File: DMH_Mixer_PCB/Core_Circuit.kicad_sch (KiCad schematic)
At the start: 31 parts, among them SW1 SW_SPDT_321, SW2 SW_SPDT_321, SW3 SW_SPDT_321, SW4 SW_SPDT_321, SW5 SW_DPDT, U1 TL072

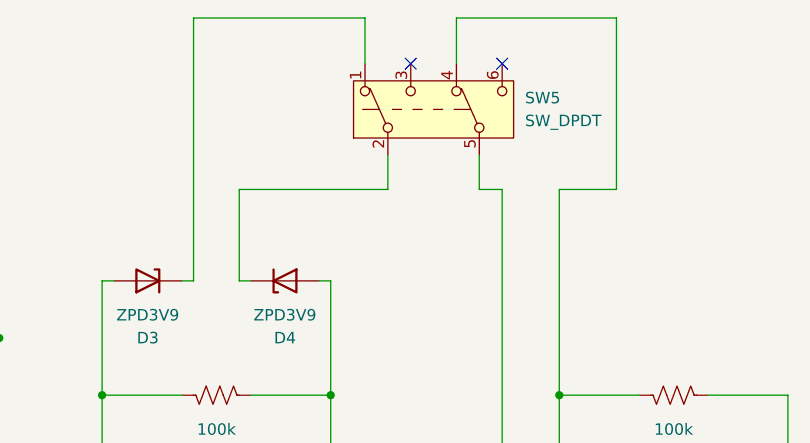
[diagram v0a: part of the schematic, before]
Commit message: PCB Component placement ready
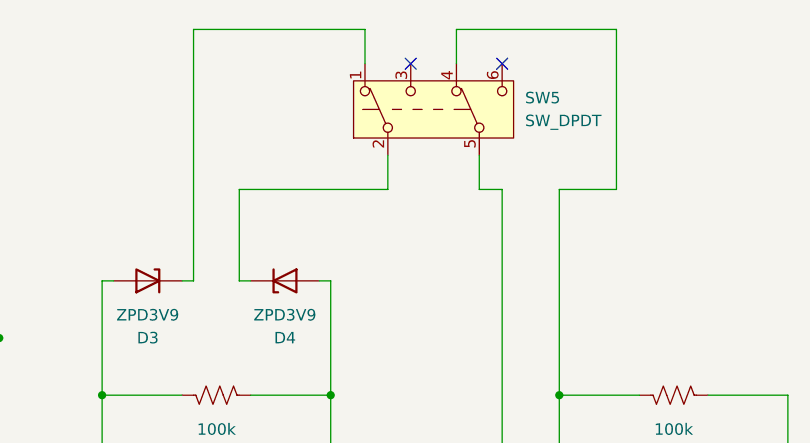
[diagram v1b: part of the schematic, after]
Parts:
- SW5: footprint SynthStuff:PinHeader_2x03_P2.54mm_Vertical_142536 -> SynthStuff:Toggle_Switch_2_Poles_THT
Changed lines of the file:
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@@
 	(wire
 		(pts
-			(xy 165.1 59.69) (xy 165.1 40.64)
+			(xy 165.1 59.69) (xy 165.1 41.91)
 		)
 		(stroke
@@
 	(wire
 		(pts
-			(xy 165.1 40.64) (xy 147.32 40.64)
+			(xy 165.1 41.91) (xy 147.32 41.91)
 		)
 		(stroke
@@
 	(wire
 		(pts
-			(xy 147.32 40.64) (xy 147.32 45.72)
+			(xy 147.32 41.91) (xy 147.32 45.72)
 		)
 		(stroke
@@
 	(wire
 		(pts
-			(xy 118.11 40.64) (xy 137.16 40.64)
+			(xy 118.11 41.91) (xy 137.16 41.91)
 		)
 		(stroke
@@
 	(wire
 		(pts
-			(xy 118.11 40.64) (xy 118.11 69.85)
+			(xy 118.11 41.91) (xy 118.11 69.85)
 		)
 		(stroke
@@
 	(wire
 		(pts
-			(xy 137.16 40.64) (xy 137.16 45.72)
+			(xy 137.16 41.91) (xy 137.16 45.72)
 		)
 		(stroke
@@
 			)
 		)
-		(property "Footprint" "SynthStuff:PinHeader_2x03_P2.54mm_Vertical_142536"
+		(property "Footprint" "SynthStuff:Toggle_Switch_2_Poles_THT"
 			(at 139.7 50.8 0)
 			(effects
@@
 			)
 		)
+		(property "Function" ""
+			(at 144.78 50.8 0)
+			(effects
+				(font
+					(size 1.27 1.27)
+				)
+			)
+		)
